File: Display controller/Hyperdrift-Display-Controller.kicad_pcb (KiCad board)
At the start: 2 copper layers, 100 x 75 mm, 39 parts, among them J1 Panel1, J2 Panel2, J3 Panel3, J4 IIC+12V, J5 IIC+12V, J6 Conn_01x10_Pin, U1 IS31FL3733-TQ, U2 AMS1117-5.0

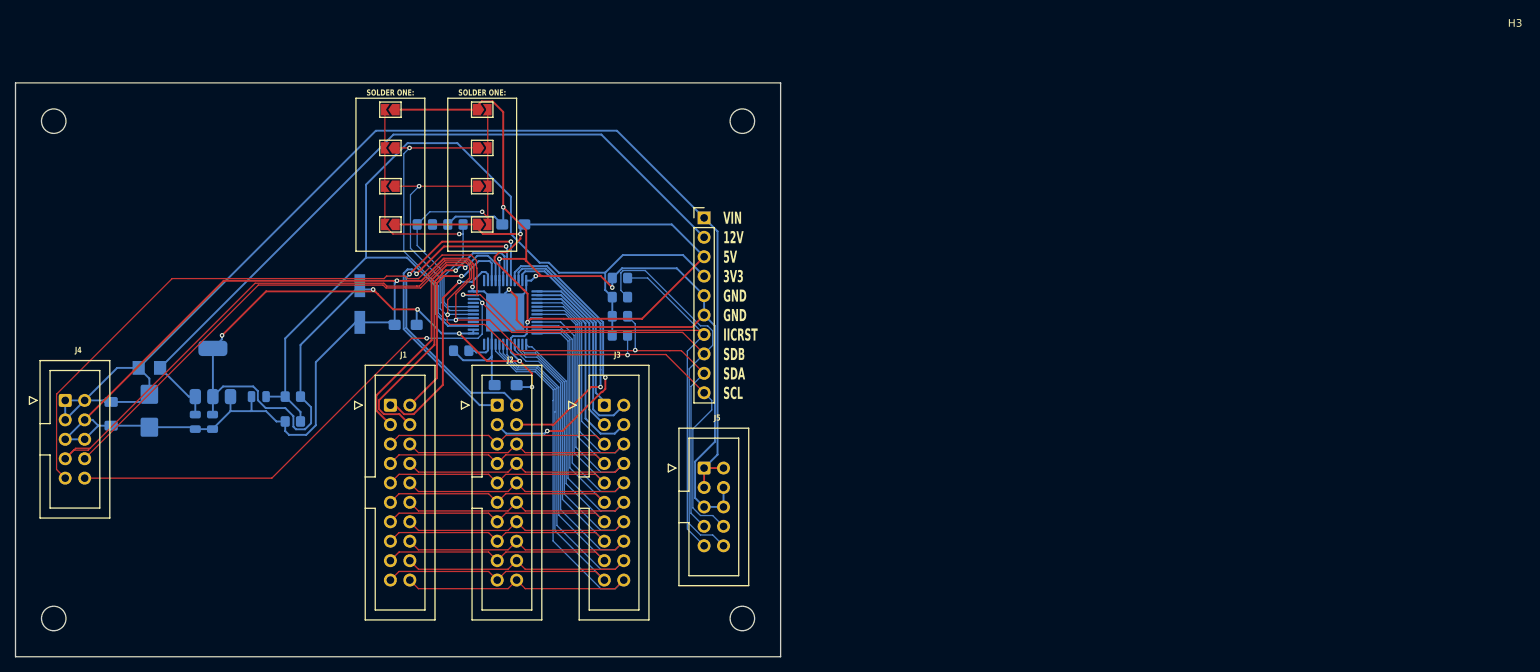
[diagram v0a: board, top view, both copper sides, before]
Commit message: Add ground pour for Hyperdrift-Display-Controller
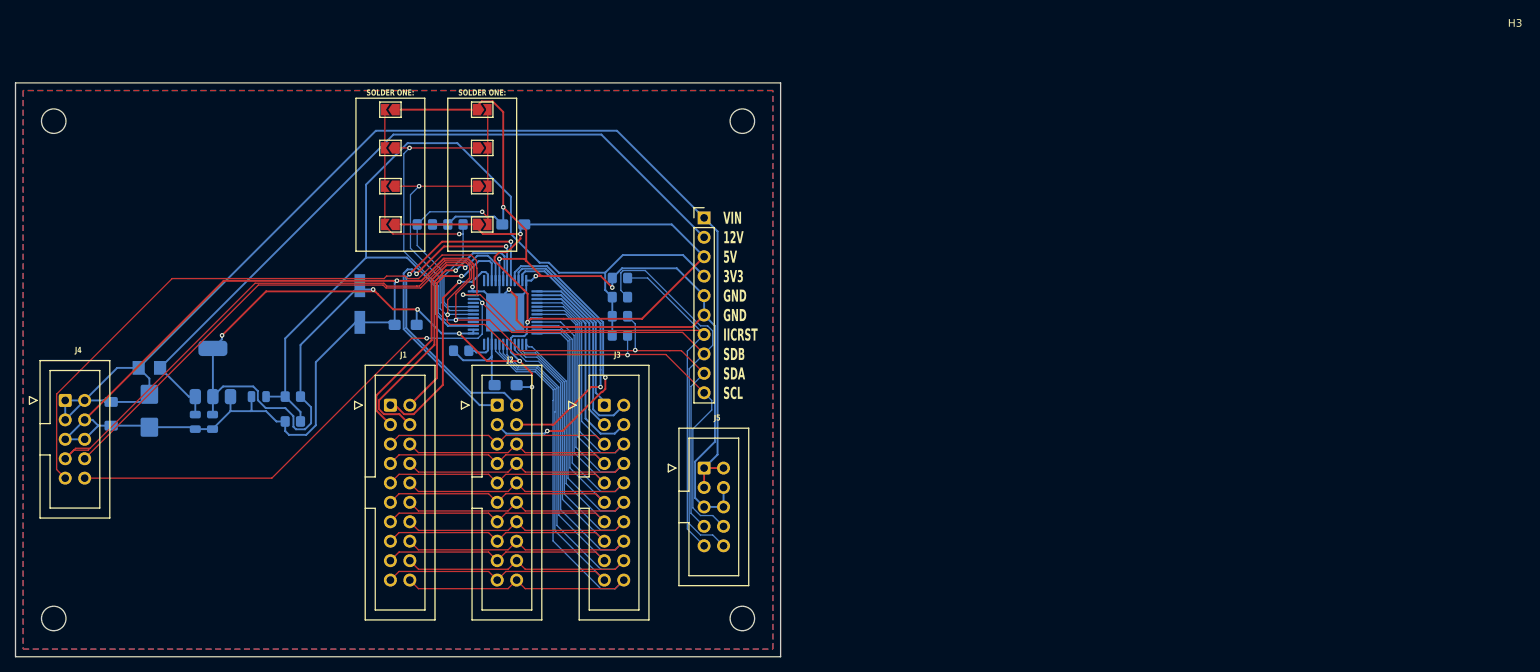
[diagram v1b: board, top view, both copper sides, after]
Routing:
- added copper zone on B.Cu, net GND
- added copper zone on F.Cu, net GND
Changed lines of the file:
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@@
 		(net 40)
+	)
+	(zone
+		(net 22)
+		(net_name "GND")
+		(layers "F.Cu" "B.Cu")
+		(name "GNDZ")
+		(hatch edge 0.5)
+		(connect_pads
+			(clearance 0.5)
+		)
+		(min_thickness 0.25)
+		(filled_areas_thickness no)
+		(fill yes
+			(thermal_gap 0.5)
+			(thermal_bridge_width 0.5)
+		)
+		(polygon
+			(pts
+				(xy 80 47.5) (xy 80 120.5) (xy 178 120.5) (xy 178 47.5)
+			)
+		)
 	)
 	(embedded_fonts no)
